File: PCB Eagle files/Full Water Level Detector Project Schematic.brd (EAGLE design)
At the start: 100 x 80 mm, 23 parts, among them IC1 74AHCT125

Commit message: PCB Layout WIP archive
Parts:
- added ELEC-LEFT, ELEC-RIGHT: (no value), con-lstb:MA06-1
- moved JP1 155.2 mm to (87.6, 64.8), turned to 180 degrees
- moved C1 131.1 mm to (78.7, 68.6)
- moved IC1 128.1 mm to (88.9, 19.1)
- moved U$1 108.5 mm to (61.0, 53.3), turned to 270 degrees
- moved EXPANSION 96.7 mm to (55.9, 68.6)
- moved J2 93.6 mm to (26.7, 72.4)
- moved U$2 87.8 mm to (39.4, 24.1)
- moved SP2 85.6 mm to (61.0, 19.1)
- moved PUSHBUTTON 53.0 mm to (-69.8, 47.0)
- moved R4 45.7 mm to (-66.0, 74.9)
- moved C4 40.6 mm to (-57.1, 81.3)
- moved C5 40.6 mm to (-62.2, 81.3)
- moved J3 36.8 mm to (-54.6, 68.6)
- moved J1 23.3 mm to (-34.3, 68.6)
- moved C3 16.5 mm to (-52.1, 81.3)
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
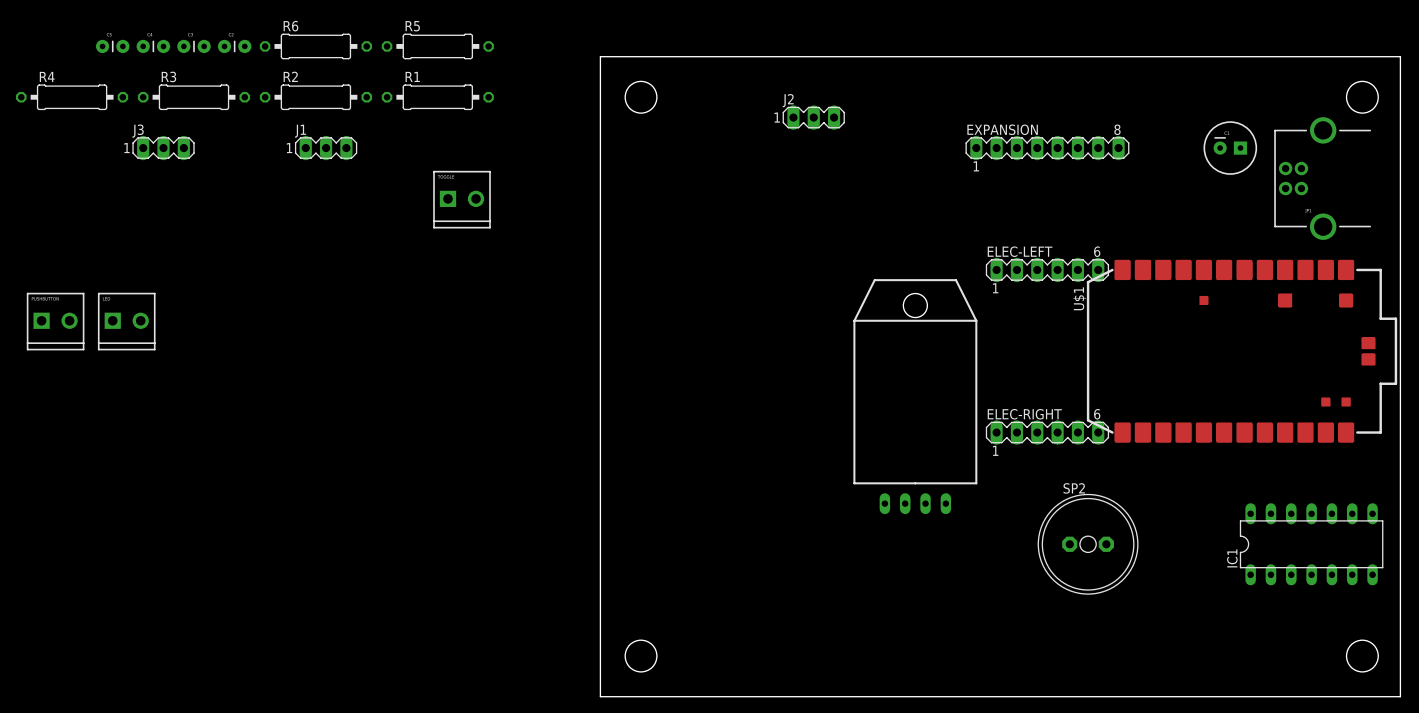
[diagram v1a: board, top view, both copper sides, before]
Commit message: Updated schematic
Changed mini screw terminals to pin headers.  Completed board placement
and routing, but still need the ground pour.
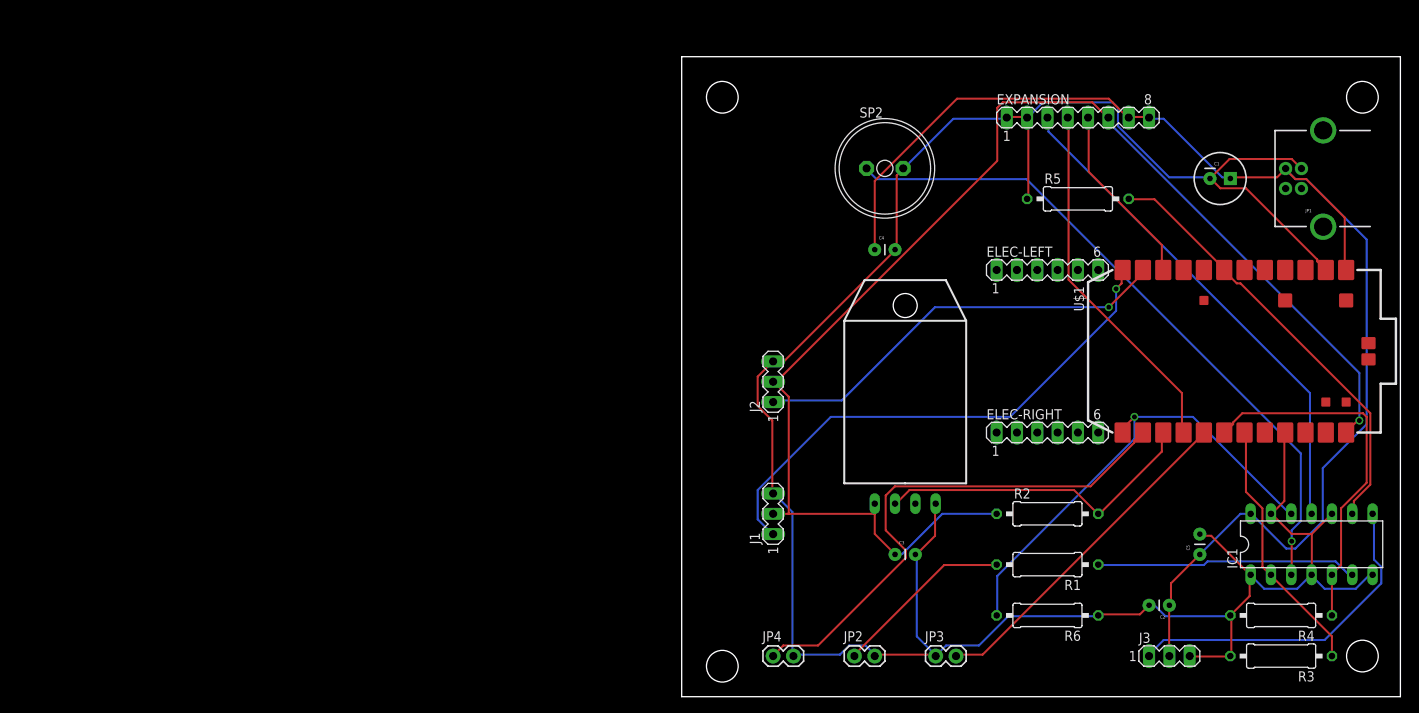
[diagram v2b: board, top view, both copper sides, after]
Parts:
- removed LED, PUSHBUTTON, TOGGLE: M023.5MM, SparkFun-Connectors:SCREWTERMINAL-3.5MM-2
- added JP2, JP3, JP4: M02PTH, SparkFun-Connectors:1X02
- J1: value (none) -> Sensor 1
- J2: value (none) -> Sensor 2
- J3: value (none) -> Servo
- moved R4 164.4 mm to (85.1, 10.2), turned to 180 degrees
- moved R3 152.8 mm to (85.1, 5.08), turned to 180 degrees
- moved C5 151.1 mm to (74.9, 17.8), turned to 90 degrees
- moved J3 140.9 mm to (71.1, 5.08)
- moved C2 137.2 mm to (71.1, 11.4), turned to 180 degrees
- moved R6 115.8 mm to (55.9, 10.2), turned to 180 degrees
- moved C3 109.2 mm to (36.8, 17.8)
- moved R2 105.2 mm to (55.9, 22.9)
- moved R1 96.0 mm to (55.9, 16.5), turned to 180 degrees
- moved C4 94.9 mm to (34.3, 55.9)
- moved R5 82.2 mm to (59.7, 62.2)
- moved J1 72.2 mm to (21.6, 22.9), turned to 90 degrees
- moved SP2 53.4 mm to (35.6, 66.0)
- moved J2 33.4 mm to (21.6, 39.4), turned to 90 degrees
- moved EXPANSION 5.39 mm to (59.7, 72.4)
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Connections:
- net GND: now also JP2.2, JP3.1, JP4.2; no longer LED.2, PUSHBUTTON.1, TOGGLE.2
- net N$10: now also JP2.1; no longer LED.1
- net N$11: now also JP3.2; no longer PUSHBUTTON.2
- net N$22: now also JP4.1; no longer TOGGLE.1
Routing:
- net GND: track 0.00 -> 310.3 mm
- net VCC: track 0.00 -> 172.2 mm
- net +3.3V: track 0.00 -> 166.6 mm, vias 0 -> 1
- net N$6: track 0.00 -> 84.7 mm, vias 0 -> 1
- net N$22: track 0.00 -> 66.1 mm
- net N$3: track 0.00 -> 65.9 mm, vias 0 -> 1
- net N$15: track 0.00 -> 63.3 mm
- net N$17: track 0.00 -> 59.1 mm, vias 0 -> 1
- net N$7: track 0.00 -> 55.1 mm
- net N$2: track 0.00 -> 53.3 mm, vias 0 -> 1
- net N$23: track 0.00 -> 45.7 mm
- net N$14: track 0.00 -> 45.4 mm
- net N$11: track 0.00 -> 42.6 mm
- net N$1: track 0.00 -> 42.1 mm
- net N$19: track 0.00 -> 41.0 mm
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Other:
- board size 100 x 80 mm -> 89.8 x 80 mm

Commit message: Optimized and routed PCB
Still must perform the ground pour and create silk screen.
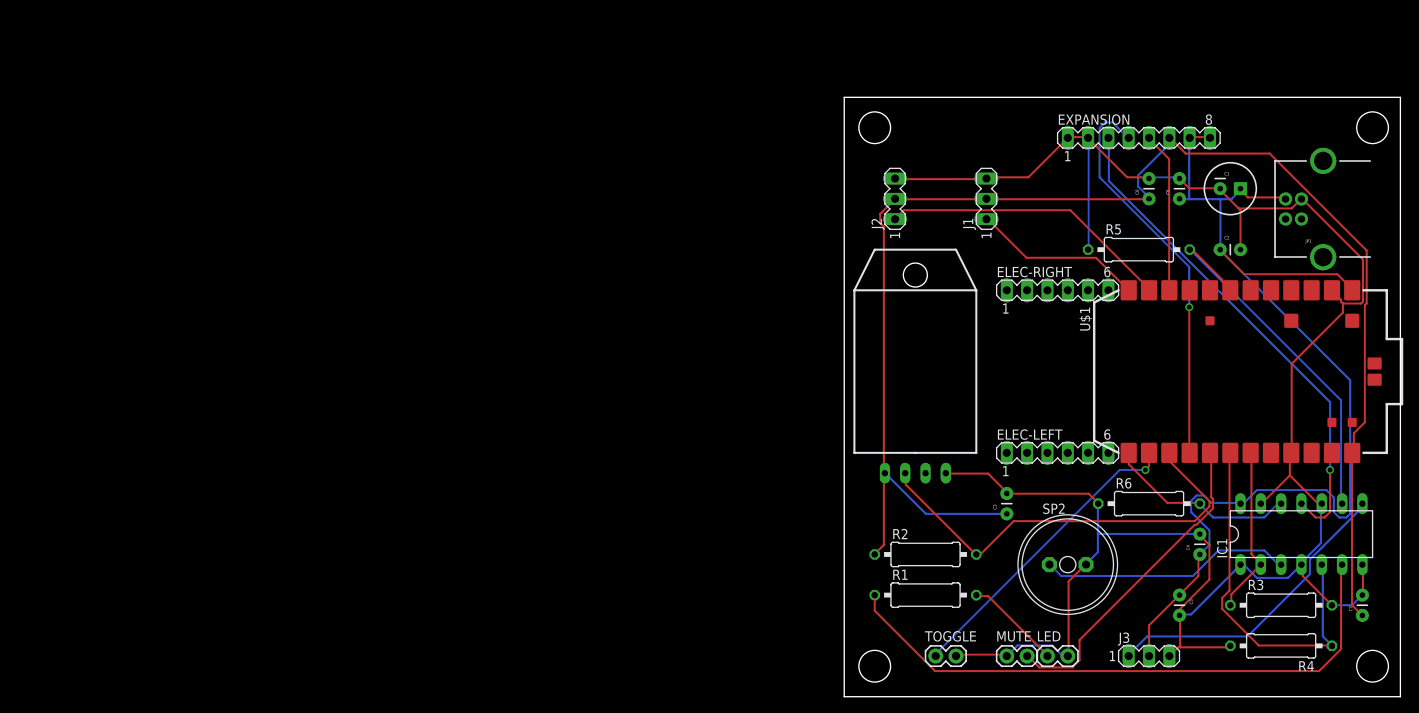
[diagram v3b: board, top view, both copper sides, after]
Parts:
- removed JP2, JP4: M02PTH, SparkFun-Connectors:1X02
- added C6, C7, C8: 0.1 uF, SparkFun-Passives:CAP-PTH-SMALL
- added LED, MUTE: M02PTH, SparkFun-Connectors:1X02
- moved C4 55.7 mm to (74.9, 17.8), turned to 90 degrees
- moved SP2 54.6 mm to (58.4, 16.5)
- moved J1 47.6 mm to (48.3, 62.2)
- moved C2 44.9 mm to (77.5, 55.9), turned to 0 degrees
- moved J2 27.5 mm to (36.8, 62.2)
- moved ELEC-LEFT 22.9 mm to (57.1, 30.5)
- moved R6 18.9 mm to (68.6, 24.1), turned to 0 degrees
- moved ELEC-RIGHT 17.8 mm to (57.1, 50.8)
- moved R2 16.1 mm to (40.6, 17.8)
- moved R1 15.7 mm to (40.6, 12.7), turned to 0 degrees
- moved C3 14.9 mm to (50.8, 22.9), turned to 90 degrees
- moved R5 9.92 mm to (67.3, 55.9)
- moved EXPANSION 8.03 mm to (67.3, 69.8)
- moved R3 6.35 mm to (85.1, 11.4), turned to 0 degrees
- moved C5 5.68 mm to (72.4, 12.7), turned to 270 degrees
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- renumbered JP3 to TOGGLE
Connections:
- net +3.3V: now also C7.1, C8.1
- net GND: now also C6.2, C7.2, C8.2, LED.2, MUTE.1, TOGGLE.2; no longer JP2.2, JP4.2, TOGGLE.1
- net N$10: now also LED.1; no longer JP2.1
- net N$11: now also MUTE.2; no longer TOGGLE.2
- net N$22: now also TOGGLE.1; no longer JP4.1
- net VCC: now also C6.1
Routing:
- net N$6: track 84.7 -> 31.7 mm, vias 1 -> 0
- net N$3: track 65.9 -> 21.4 mm, vias 1 -> 0
- net N$9: track 32.7 -> 75.2 mm
- net GND: track 310.3 -> 269.2 mm
- net N$17: track 59.1 -> 24.0 mm, vias 1 -> 0
- net VCC: track 172.2 -> 137.1 mm
- net N$22: track 66.1 -> 38.4 mm, vias 0 -> 1
- net N$2: track 53.3 -> 36.5 mm, vias 1 -> 0
- net +3.3V: track 166.6 -> 182.4 mm, vias 1 -> 0
- net N$19: track 41.0 -> 54.3 mm
- net N$4: track 32.5 -> 21.2 mm
- net N$10: track 22.6 -> 12.1 mm
- net N$7: track 55.1 -> 47.1 mm
- net N$14: track 45.4 -> 50.0 mm, vias 0 -> 1
- net N$1: track 42.1 -> 38.5 mm
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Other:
- board size 89.8 x 80 mm -> 69.5 x 74.9 mm
